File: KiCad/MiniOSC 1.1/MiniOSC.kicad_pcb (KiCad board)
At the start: 2 copper layers, 94.1 x 128.5 mm, 58 parts, among them J1 Conn_01x16_Female, J2 Conn_01x16_Male, J3 V_OCT_IN, J4 FM_IN, J5 PULSE_OUT, J6 SAW_OUT, J7 JST_BUS, J8 IDC_BUS, Q1 BC558, Q2 BC548, U1 TL074, U2 40106

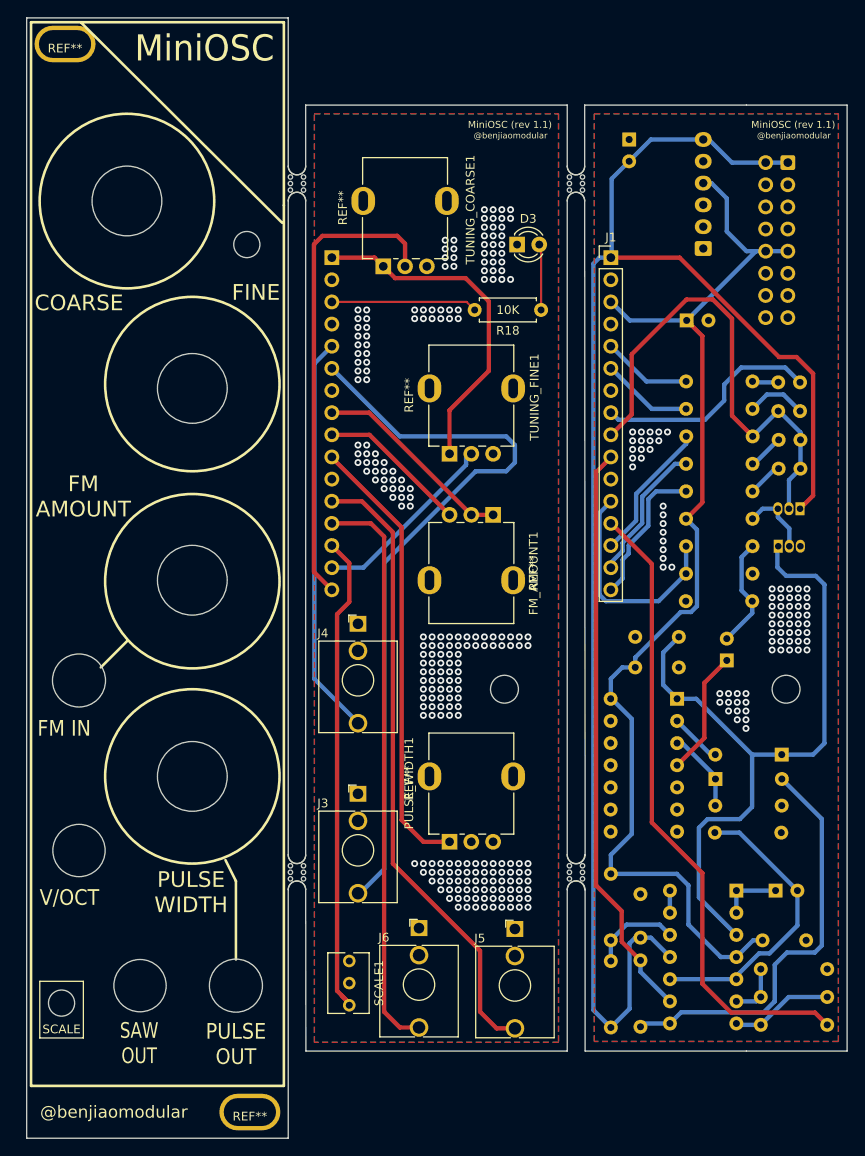
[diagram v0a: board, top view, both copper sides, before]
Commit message: some clean up v1.1 combined boards version changes r14 silkscreen switched + misc silkscreen fixes turned on teardrops output gerbers ouput bom
then created handscore version - low cost
adjusted routing to keep traces further from scored / break edges
included teardrops
then ouput gerbeeres + bom +
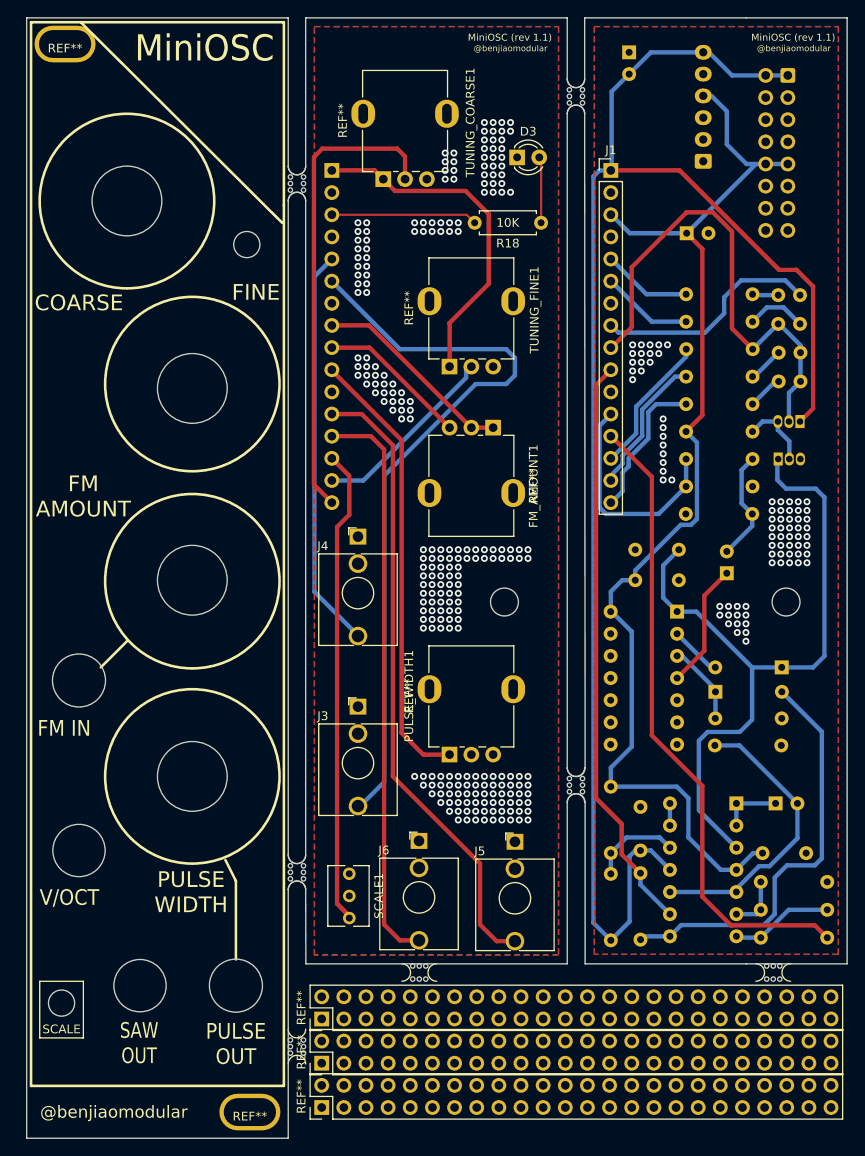
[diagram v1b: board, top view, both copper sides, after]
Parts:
- removed the mouse-bite-2mm-slot at (103.0, 64.0)
- added REF**: PinHeader_2x24_P2.54mm_Vertical, Connector_PinHeader_2.54mm:PinHeader_2x24_P2.54mm_Vertical, F.Cu at (73.8, 164.9)
- added REF**: PinHeader_2x24_P2.54mm_Vertical, Connector_PinHeader_2.54mm:PinHeader_2x24_P2.54mm_Vertical, F.Cu at (73.8, 159.8)
- added REF**: PinHeader_2x24_P2.54mm_Vertical, Connector_PinHeader_2.54mm:PinHeader_2x24_P2.54mm_Vertical, F.Cu at (73.8, 170.0)
- added mouse-bite-2mm-slot: VAL**, Panelization:mouse-bite-2mm-slot, F.Cu at (125.6, 154.5)
- added mouse-bite-2mm-slot: VAL**, Panelization:mouse-bite-2mm-slot, F.Cu at (85.0, 154.5)
- added mouse-bite-2mm-slot: VAL**, Panelization:mouse-bite-2mm-slot, F.Cu at (71.0, 163.0)
- added mouse-bite-2mm-slot: VAL**, Panelization:mouse-bite-2mm-slot, F.Cu at (103.0, 54.0)
- moved D2 10.0 mm to (119.0, 122.3)
- moved C1 10.0 mm to (114.8, 106.0)
- moved C2 10.0 mm to (125.9, 135.1)
- moved C3 10.0 mm to (120.3, 108.7)
- moved C4 10.0 mm to (115.7, 69.7)
- moved C5 10.0 mm to (109.1, 49.0)
- moved C6 10.0 mm to (109.8, 109.5)
- moved C7 10.0 mm to (124.4, 140.8)
- moved C8 10.0 mm to (110.4, 135.5)
- moved D1 10.0 mm to (126.6, 119.5)
- moved D3 10.0 mm to (96.2, 61.0)
- moved FM_AMOUNT1 10.0 mm to (93.5, 92.0)
- moved J1 10.0 mm to (107.0, 62.5)
- moved J2 10.0 mm to (75.0, 62.5)
- moved J3 10.0 mm to (78.0, 124.0)
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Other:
- outline, holes or cut-outs redrawn
- net class Default removed
